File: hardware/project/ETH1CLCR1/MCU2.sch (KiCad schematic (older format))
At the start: 28 parts, among them J1501 Conn_02x05, U1502 24LC08B-E/MS, U501 STM32H743ZI, Y1501 NX3225GD-8MHZ-STD-CRA-3

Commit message: Schematic design
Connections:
- net labels added: SR100CTR, SR10CTR, SR10KCTR, SR1KCTR
- net labels removed: ADC_BUSY, ADC_CLOCK, ADC_CONVST, ADC_MUX_DIN, ADC_MUX_SCLK, ADC_MUX_SDO, ADC_MUX_~SYNC, ADC_RD, ADC_SDI, ADC_SDOA, ADC_~CS, DAC_RSTSEL, DAC_SCLK, DAC_SDIN, DAC_SDO, DAC_~LDAC, DAC_~RESET, DAC_~SYNC, DC_DAC_SCLK, DC_DAC_SDIN, DC_DAC_SDO, DC_DAC_~CLR, DC_DAC_~LDAC, DC_DAC_~SYNC, FOURCE_SELECT, PMU_AC0, PMU_AC1, PMU_AM0, PMU_AM1, PMU_AM2, PMU_CLHDETECT, PMU_CLLDETECT, PMU_CPCK, PMU_CPOH, PMU_CPOL, PMU_CPSEL, PMU_MSEL, PMU_STANDBY, PMU_~CS, PMU_~MOE, PMU_~STB, R_GND, R_GUARD, R_GUARDIN, R_MEASHV, R_MEASIL, R_MEASVL
- wire segments 225 -> 229
- no-connect marks 53 -> 49
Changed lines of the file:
@@
 $Descr A3 16535 11693
 encoding utf-8
-Sheet 6 12
+Sheet 12 13
 Title ""
 Date ""
@@
 Wire Wire Line
 	2900 6300 2850 6300
-Text HLabel 2850 2000 0    50   Output ~ 0
-DC_DAC_~CLR
-Text HLabel 2850 2100 0    50   Output ~ 0
-DC_DAC_~LDAC
-Text HLabel 2850 2400 0    50   Input ~ 0
-DC_DAC_SDO
-Text HLabel 2850 2200 0    50   Output ~ 0
-DC_DAC_~SYNC
-Text HLabel 2850 2300 0    50   Output ~ 0
-DC_DAC_SCLK
-Text HLabel 2850 2500 0    50   Output ~ 0
-DC_DAC_SDIN
 Wire Wire Line
 	2850 2300 2900 2300
@@
 Wire Wire Line
 	2850 2100 2900 2100
-Text HLabel 2850 3900 0    50   Input ~ 0
-ADC_SDOA
-Text HLabel 2850 5400 0    50   Output ~ 0
-ADC_RD
-Text HLabel 2850 4000 0    50   Output ~ 0
-ADC_SDI
-Text HLabel 2850 5500 0    50   Input ~ 0
-ADC_BUSY
-Text HLabel 2850 3800 0    50   Output ~ 0
-ADC_CLOCK
 Wire Wire Line
 	2850 3800 2900 3800
@@
 Text Label 15700 8400 2    50   ~ 0
 MCU_NRST
-Text HLabel 14350 7900 2    50   Output ~ 0
-ADC_MUX_DIN
-Text HLabel 14350 7600 2    50   Output ~ 0
-ADC_MUX_~SYNC
-Text HLabel 14350 7400 2    50   Output ~ 0
-ADC_MUX_SCLK
-Text HLabel 14350 7800 2    50   Input ~ 0
-ADC_MUX_SDO
 Wire Wire Line
 	14350 7600 14300 7600
@@
 Wire Wire Line
 	14300 3700 14350 3700
-Text HLabel 2850 6200 0    50   Output ~ 0
-DAC_SDIN
-Text HLabel 2850 6000 0    50   Output ~ 0
-DAC_SCLK
-Text HLabel 2850 4800 0    50   Output ~ 0
-DAC_~SYNC
 Wire Wire Line
 	1500 1400 2900 1400
-Text HLabel 14350 3800 2    50   Output ~ 0
-PMU_STANDBY
-Text HLabel 14350 3900 2    50   Output ~ 0
-PMU_~STB
-Text HLabel 14350 4000 2    50   Output ~ 0
-PMU_CPCK
-Text HLabel 14350 4100 2    50   Output ~ 0
-PMU_~MOE
-Text HLabel 14350 4200 2    50   Output ~ 0
-PMU_~CS
-Text HLabel 14350 4300 2    50   Output ~ 0
-PMU_AM0
-Text HLabel 14350 4400 2    50   Output ~ 0
-PMU_AM1
-Text HLabel 14350 4500 2    50   Output ~ 0
-PMU_AM2
-Text HLabel 14350 5400 2    50   Output ~ 0
-PMU_CPSEL
-Text HLabel 14350 5500 2    50   Output ~ 0
-PMU_MSEL
-Text HLabel 14350 5600 2    50   Output ~ 0
-PMU_AC0
-Text HLabel 14350 5700 2    50   Output ~ 0
-PMU_AC1
-Text HLabel 14350 5800 2    50   Input ~ 0
-PMU_CPOH
-Text HLabel 14350 5900 2    50   Input ~ 0
-PMU_CPOL
-Text HLabel 14350 6000 2    50   Input ~ 0
-PMU_CLHDETECT
-Text HLabel 14350 6100 2    50   Input ~ 0
-PMU_CLLDETECT
-Text HLabel 14350 1900 2    50   Output ~ 0
-R_MEASIL
-Text HLabel 14350 2000 2    50   Output ~ 0
-R_MEASVL
-Text HLabel 14350 2100 2    50   Output ~ 0
-R_GUARD
-Text HLabel 14350 1600 2    50   Output ~ 0
-R_MEASHV
-Text HLabel 14350 1700 2    50   Output ~ 0
-R_GUARDIN
-Text HLabel 14350 1800 2    50   Output ~ 0
-R_GND
 Wire Wire Line
 	14350 3800 14300 3800
@@
 NoConn ~ 11200 10450
 NoConn ~ 11200 10550
-Text HLabel 14350 6200 2    50   Output ~ 0
-FOURCE_SELECT
 Wire Wire Line
 	14350 6200 14300 6200
@@
 NoConn ~ 2900 4100
 NoConn ~ 2900 4200
-NoConn ~ 2900 5000
-NoConn ~ 2900 5100
-NoConn ~ 2900 5200
-NoConn ~ 2900 5300
 NoConn ~ 2900 5600
 NoConn ~ 2900 5700
@@
 $EndComp
 NoConn ~ 14300 7300
-Text HLabel 2850 4500 0    50   Output ~ 0
-DAC_~RESET
-Text HLabel 2850 4400 0    50   Output ~ 0
-DAC_~LDAC
 Wire Wire Line
 	2850 3700 2900 3700
-Text HLabel 2850 3700 0    50   Output ~ 0
-ADC_~CS
-Text HLabel 2850 6100 0    50   Input ~ 0
-DAC_SDO
 Wire Wire Line
 	2850 6100 2900 6100
@@
 Wire Wire Line
 	2850 4400 2900 4400
-Text HLabel 2850 4300 0    50   Output ~ 0
-DAC_RSTSEL
 Wire Wire Line
 	2850 4300 2900 4300
@@
 Wire Wire Line
 	2850 8600 2900 8600
-Text HLabel 14350 6400 2    50   Output ~ 0
-ADC_CONVST
 Wire Wire Line
 	14350 6400 14300 6400
 NoConn ~ 14300 6500
+Text HLabel 2850 5100 0    50   Output ~ 0
+SR1KCTR
+Text HLabel 2850 5000 0    50   Output ~ 0
+SR10KCTR
+Text HLabel 2850 5300 0    50   Output ~ 0
+SR10CTR
+Text HLabel 2850 5200 0    50   Output ~ 0
+SR100CTR
+Wire Wire Line
+	2850 5300 2900 5300
+Wire Wire Line
+	2900 5200 2850 5200
+Wire Wire Line
+	2850 5100 2900 5100
+Wire Wire Line
+	2900 5000 2850 5000
 $EndSCHEMATC

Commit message: Schematic design
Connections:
- net labels added: +3.3VP, ADC_BUSY, ADC_CLOCK, ADC_CONVST, ADC_NULL1, ADC_NULL2, ADC_RD, ADC_SDI, ADC_SDOA, ADC_~CS, CXN_RELA, CXN_RELB, CXN_RELC, CXN_RELD, CXN_RELE, CXN_RELF, DAC1_LDAC, DAC1_~ENABLE, DAC2_LDAC, DAC2_~ENABLE, DAC_DIN, DAC_SCLK, DAC_~SYNC, FB_CLK, FB_RDY, FB_SDI, FB_SDO, FB_~CS, FB_~RST, G1A0_CTR, G1A1_CTR, G2A0_CTR, G2A1_CTR, HA3-COMP, PA_50MV, PA_EM, PA_MOS1, PA_MOS2, PA_MOS3, PA_MOS4, PA_MOS5, PA_MOS6, PA_NULL, R100CRT, R100KCRT, R10CRT, R10KCRT, R1KCRT, RELAY_CTR, RR_CLK, RR_RDY, RR_SDI, RR_SDO, RR_~CS, RR_~RST
- wire segments 229 -> 233
- no-connect marks 49 -> 45
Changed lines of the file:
@@
 $Descr A3 16535 11693
 encoding utf-8
-Sheet 12 14
+Sheet 11 16
 Title ""
 Date ""
@@
 Comment4 ""
 $EndDescr
-$Comp
-L ETH1CLCR1:STM32H743ZI U501
-U 1 1 5DD1F48B
-P 8600 5050
-F 0 "U501" H 3150 8950 50  0000 C CNN
-F 1 "STM32H743ZI" H 13850 8950 50  0000 C CNN
-F 2 "ETH1CLCR1:TQFP-144_20x20mm_P0.5mm" H 24500 6550 50  0001 C CNN
-F 3 "" H 24500 6550 50  0001 C CNN
-	1    8600 5050
-	1    0    0    -1
-$EndComp
-$Comp
-L ETH1CLCR1:+3.3VF #PWR0501
-U 1 1 5DD24561
-P 8600 900
-F 0 "#PWR0501" H 8600 750 50  0001 C CNN
-F 1 "+3.3VF" H 8615 1073 50  0000 C CNN
-F 2 "" H 8600 900 50  0001 C CNN
-F 3 "" H 8600 900 50  0001 C CNN
-	1    8600 900
-	1    0    0    -1
-$EndComp
 Wire Wire Line
 	7400 1000 7400 950
@@
 F 3 "" H 10550 10700 50  0001 C CNN
 	1    10550 10700
-	1    0    0    -1
-$EndComp
-$Comp
-L ETH1CLCR1:+3.3VF #PWR0512
-U 1 1 5DD9082D
-P 10550 10150
-F 0 "#PWR0512" H 10550 10000 50  0001 C CNN
-F 1 "+3.3VF" H 10565 10323 50  0000 C CNN
-F 2 "" H 10550 10150 50  0001 C CNN
-F 3 "" H 10550 10150 50  0001 C CNN
-	1    10550 10150
 	1    0    0    -1
 $EndComp
@@
 $EndComp
 $Comp
-L ETH1CLCR1:+3.3VF #PWR0513
-U 1 1 5E23D8BE
-P 8500 10200
-F 0 "#PWR0513" H 8500 10050 50  0001 C CNN
-F 1 "+3.3VF" H 8515 10373 50  0000 C CNN
-F 2 "" H 8500 10200 50  0001 C CNN
-F 3 "" H 8500 10200 50  0001 C CNN
-	1    8500 10200
-	1    0    0    -1
-$EndComp
-$Comp
-L ETH1CLCR1:+3.3VF #PWR0511
-U 1 1 5E23DAAC
-P 9800 9950
-F 0 "#PWR0511" H 9800 9800 50  0001 C CNN
-F 1 "+3.3VF" H 9815 10123 50  0000 C CNN
-F 2 "" H 9800 9950 50  0001 C CNN
-F 3 "" H 9800 9950 50  0001 C CNN
-	1    9800 9950
-	1    0    0    -1
-$EndComp
-$Comp
 L Device:C C?
 U 1 1 5E25BB78
@@
 Wire Wire Line
 	3400 10450 3650 10450
-$Comp
-L ETH1CLCR1:+3.3VF #PWR0515
-U 1 1 5DFCC179
-P 3400 10400
-F 0 "#PWR0515" H 3400 10250 50  0001 C CNN
-F 1 "+3.3VF" H 3415 10573 50  0000 C CNN
-F 2 "" H 3400 10400 50  0001 C CNN
-F 3 "" H 3400 10400 50  0001 C CNN
-	1    3400 10400
-	1    0    0    -1
-$EndComp
 $Comp
 L ETH1CLCR1:DGNDF #PWR0520
@@
 Wire Wire Line
 	14350 7800 14300 7800
-$Comp
-L ETH1CLCR1:+3.3VF #PWR0503
-U 1 1 5E8AA48C
-P 15200 8050
-F 0 "#PWR0503" H 15200 7900 50  0001 C CNN
-F 1 "+3.3VF" H 15215 8223 50  0000 C CNN
-F 2 "" H 15200 8050 50  0001 C CNN
-F 3 "" H 15200 8050 50  0001 C CNN
-	1    15200 8050
-	1    0    0    -1
-$EndComp
 Wire Wire Line
 	14350 7900 14300 7900
@@
 Wire Wire Line
 	15200 8400 14300 8400
-NoConn ~ 2900 1600
-NoConn ~ 2900 1700
-NoConn ~ 2900 1800
-NoConn ~ 2900 1900
 NoConn ~ 2900 2600
 NoConn ~ 2900 2700
@@
 MCU_VDDA
 $Comp
-L ETH1CLCR1:+3.3VF #PWR0514
-U 1 1 5E2EEABF
-P 6600 10350
-F 0 "#PWR0514" H 6600 10200 50  0001 C CNN
-F 1 "+3.3VF" H 6615 10523 50  0000 C CNN
-F 2 "" H 6600 10350 50  0001 C CNN
-F 3 "" H 6600 10350 50  0001 C CNN
-	1    6600 10350
-	1    0    0    -1
-$EndComp
-$Comp
 L ETH1CLCR1:DGNDF #PWR0517
 U 1 1 5E2F2EC2
@@
 Wire Wire Line
 	2900 5000 2850 5000
+$Comp
+L power:+3.3VP #PWR01203
+U 1 1 5E6F8C8C
+P 8600 900
+F 0 "#PWR01203" H 8750 850 50  0001 C CNN
+F 1 "+3.3VP" H 8620 1043 50  0000 C CNN
+F 2 "" H 8600 900 50  0001 C CNN
+F 3 "" H 8600 900 50  0001 C CNN
+	1    8600 900
+	1    0    0    -1
+$EndComp
+$Comp
+L power:+3.3VP #PWR01216
+U 1 1 5E6F95E8
+P 15200 8050
+F 0 "#PWR01216" H 15350 8000 50  0001 C CNN
+F 1 "+3.3VP" H 15220 8193 50  0000 C CNN
+F 2 "" H 15200 8050 50  0001 C CNN
+F 3 "" H 15200 8050 50  0001 C CNN
+	1    15200 8050
+	1    0    0    -1
+$EndComp
+$Comp
+L power:+3.3VP #PWR01201
+U 1 1 5E70083D
+P 6600 10350
+F 0 "#PWR01201" H 6750 10300 50  0001 C CNN
+F 1 "+3.3VP" H 6620 10493 50  0000 C CNN
+F 2 "" H 6600 10350 50  0001 C CNN
+F 3 "" H 6600 10350 50  0001 C CNN
+	1    6600 10350
+	1    0    0    -1
+$EndComp
+$Comp
+L power:+3.3VP #PWR01202
+U 1 1 5E703151
+P 8500 10200
+F 0 "#PWR01202" H 8650 10150 50  0001 C CNN
+F 1 "+3.3VP" H 8520 10343 50  0000 C CNN
+F 2 "" H 8500 10200 50  0001 C CNN
+F 3 "" H 8500 10200 50  0001 C CNN
+	1    8500 10200
+	1    0    0    -1
+$EndComp
+$Comp
+L power:+3.3VP #PWR01205
+U 1 1 5E703CD5
+P 9800 9950
+F 0 "#PWR01205" H 9950 9900 50  0001 C CNN
+F 1 "+3.3VP" H 9820 10093 50  0000 C CNN
+F 2 "" H 9800 9950 50  0001 C CNN
+F 3 "" H 9800 9950 50  0001 C CNN
+	1    9800 9950
+	1    0    0    -1
+$EndComp
+$Comp
+L power:+3.3VP #PWR01215
+U 1 1 5E705830
+P 10550 10150
+F 0 "#PWR01215" H 10700 10100 50  0001 C CNN
+F 1 "+3.3VP" H 10570 10293 50  0000 C CNN
+F 2 "" H 10550 10150 50  0001 C CNN
+F 3 "" H 10550 10150 50  0001 C CNN
+	1    10550 10150
+	1    0    0    -1
+$EndComp
+$Comp
+L ETH1CLCR1:STM32H743ZI U501
+U 1 1 5DD1F48B
+P 8600 5050
+F 0 "U501" H 3150 8950 50  0000 C CNN
+F 1 "STM32H743ZI" H 13850 8950 50  0000 C CNN
+F 2 "ETH1CLCR1:TQFP-144_20x20mm_P0.5mm" H 24500 6550 50  0001 C CNN
+F 3 "" H 24500 6550 50  0001 C CNN
+	1    8600 5050
+	1    0    0    -1
+$EndComp
+Wire Wire Line
+	2900 1900 2850 1900
+Wire Wire Line
+	2850 1800 2900 1800
+Wire Wire Line
+	2900 1700 2850 1700
+Wire Wire Line
+	2850 1600 2900 1600
+Text HLabel 2850 1600 0    50   Output ~ 0
+CXN_RELA
+Text HLabel 2850 1700 0    50   Output ~ 0
+CXN_RELB
+Text HLabel 2850 1800 0    50   Output ~ 0
+CXN_RELC
+Text HLabel 2850 1900 0    50   Output ~ 0
+CXN_RELD
+Text HLabel 2850 2000 0    50   Output ~ 0
+CXN_RELE
+Text HLabel 2850 2100 0    50   Output ~ 0
+CXN_RELF
+Text HLabel 1050 3450 0    50   Output ~ 0
+R100CRT
+Text HLabel 1050 3350 0    50   Output ~ 0
+R10CRT
+Text HLabel 1050 3550 0    50   Output ~ 0
+R1KCRT
+Text HLabel 1050 3650 0    50   Output ~ 0
+R10KCRT
+Text HLabel 1050 3750 0    50   Output ~ 0
+R100KCRT
+Text HLabel 1050 3850 0    50   Output ~ 0
+RELAY_CTR
+Text HLabel 1050 3950 0    50   Output ~ 0
+HA3-COMP
+Text HLabel 1050 4250 0    50   Output ~ 0
+PA_NULL
+Text HLabel 1050 4350 0    50   Output ~ 0
+PA_EM
+Text HLabel 1050 4450 0    50   Output ~ 0
+PA_50MV
+Text HLabel 1050 4550 0    50   Output ~ 0
+PA_MOS1
+Text HLabel 1050 4650 0    50   Output ~ 0
+PA_MOS2
+Text HLabel 1050 4750 0    50   Output ~ 0
+PA_MOS3
+Text HLabel 1050 4850 0    50   Output ~ 0
+PA_MOS4
+Text HLabel 1050 4950 0    50   Output ~ 0
+PA_MOS5
+Text HLabel 1050 5050 0    50   Output ~ 0
+PA_MOS6
+Text HLabel 1050 5250 0    50   Output ~ 0
+DAC_~SYNC
+Text HLabel 1050 5350 0    50   Output ~ 0
+DAC_SCLK
+Text HLabel 1050 5450 0    50   Output ~ 0
+DAC_DIN
+Text HLabel 1050 5550 0    50   Output ~ 0
+DAC1_~ENABLE
+Text HLabel 1050 5650 0    50   Output ~ 0
+DAC1_LDAC
+Text HLabel 1050 5750 0    50   Output ~ 0
+DAC2_~ENABLE
+Text HLabel 1050 5850 0    50   Output ~ 0
+DAC2_LDAC
+Text HLabel 1050 6050 0    50   Output ~ 0
+G1A1_CTR
+Text HLabel 1050 6150 0    50   Output ~ 0
+G1A0_CTR
+Text HLabel 1050 6250 0    50   Output ~ 0
+G2A1_CTR
+Text HLabel 1050 6350 0    50   Output ~ 0
+G2A0_CTR
+Text HLabel 1050 6600 0    50   Output ~ 0
+ADC_NULL2
+Text HLabel 1050 6700 0    50   Output ~ 0
+ADC_NULL1
+Text HLabel 1050 7500 0    50   Output ~ 0
+ADC_CONVST
+Text HLabel 1050 6900 0    50   Output ~ 0
+ADC_~CS
+Text HLabel 1050 7000 0    50   Output ~ 0
+ADC_CLOCK
+Text HLabel 1050 7100 0    50   Input ~ 0
+ADC_BUSY
+Text HLabel 1050 7200 0    50   Output ~ 0
+ADC_SDI
+Text HLabel 1050 7300 0    50   Output ~ 0
+ADC_RD
+Text HLabel 1050 7400 0    50   Input ~ 0
+ADC_SDOA
+Text HLabel 1050 7700 0    50   Output ~ 0
+RR_SDI
+Text HLabel 1050 7800 0    50   Input ~ 0
+RR_SDO
+Text HLabel 1050 7900 0    50   Output ~ 0
+RR_CLK
+Text HLabel 1050 8000 0    50   Output ~ 0
+RR_~CS
+Text HLabel 1050 8100 0    50   Input ~ 0
+RR_RDY
+Text HLabel 1050 8200 0    50   Output ~ 0
+RR_~RST
+Text HLabel 1050 8400 0    50   Output ~ 0
+FB_SDI
+Text HLabel 1050 8500 0    50   Input ~ 0
+FB_SDO
+Text HLabel 1050 8600 0    50   Output ~ 0
+FB_CLK
+Text HLabel 1050 8700 0    50   Output ~ 0
+FB_~CS
+Text HLabel 1050 8800 0    50   Input ~ 0
+FB_RDY
+Text HLabel 1050 8900 0    50   Output ~ 0
+FB_~RST
 $EndSCHEMATC

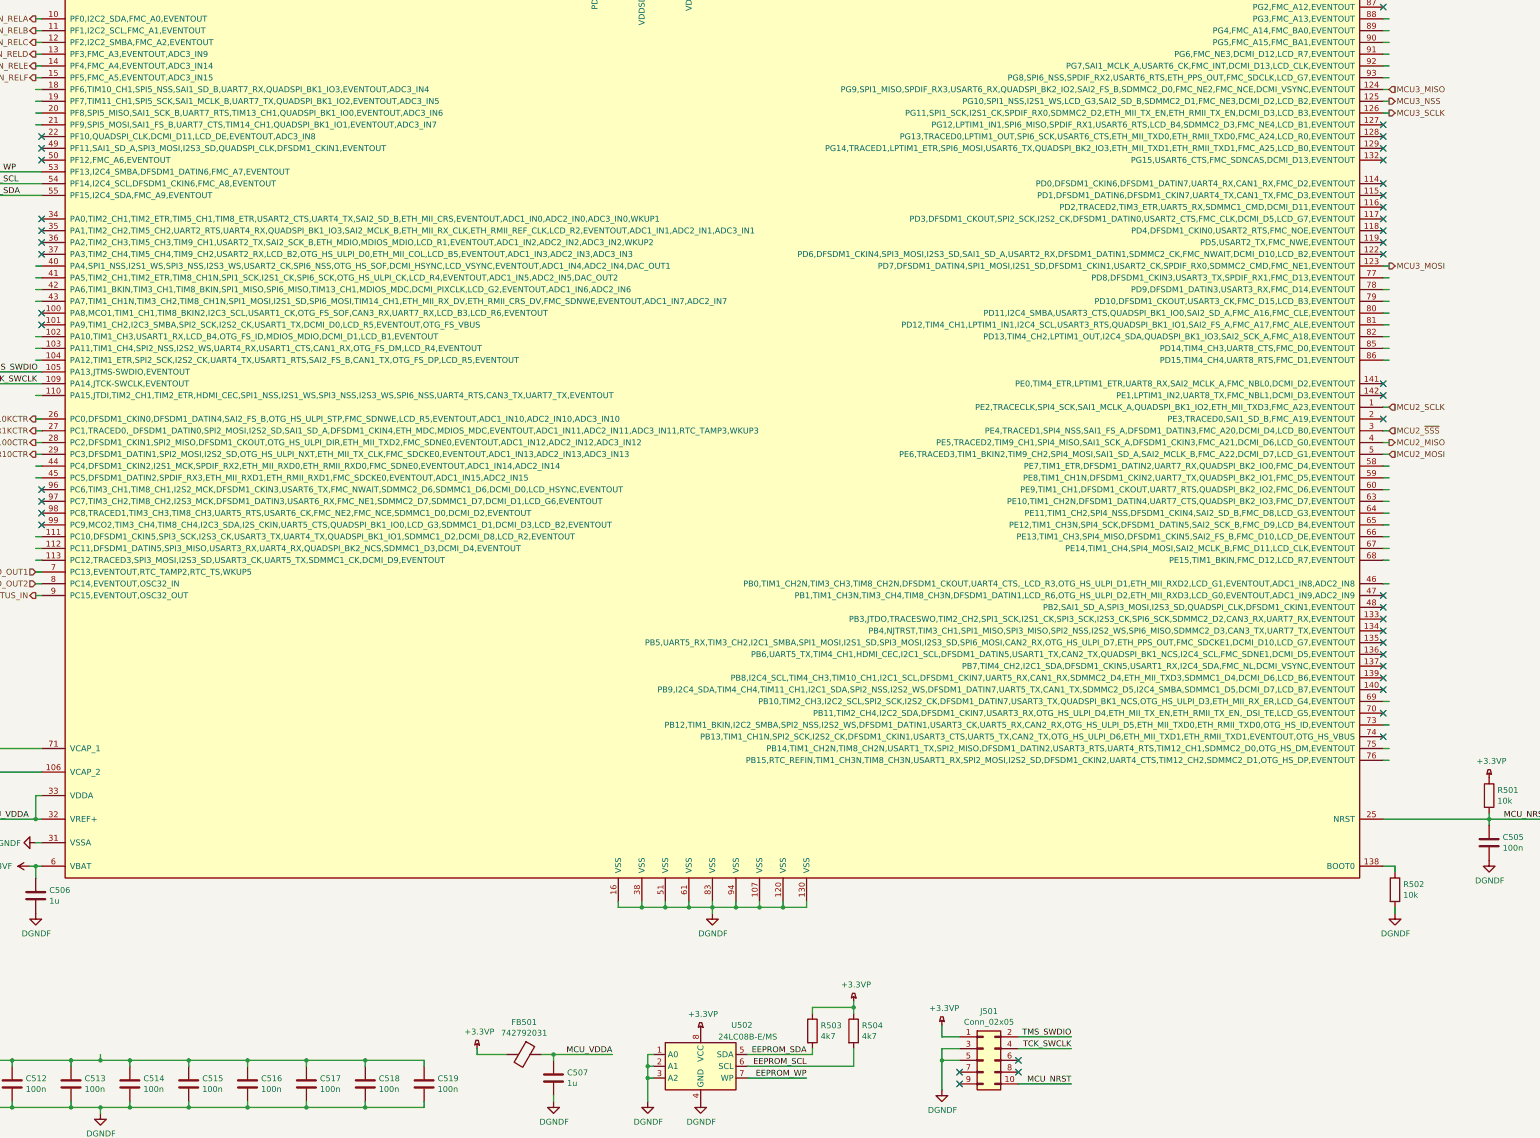
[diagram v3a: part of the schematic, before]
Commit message: Need to redesign the AC source, the LT1468 is too slow.
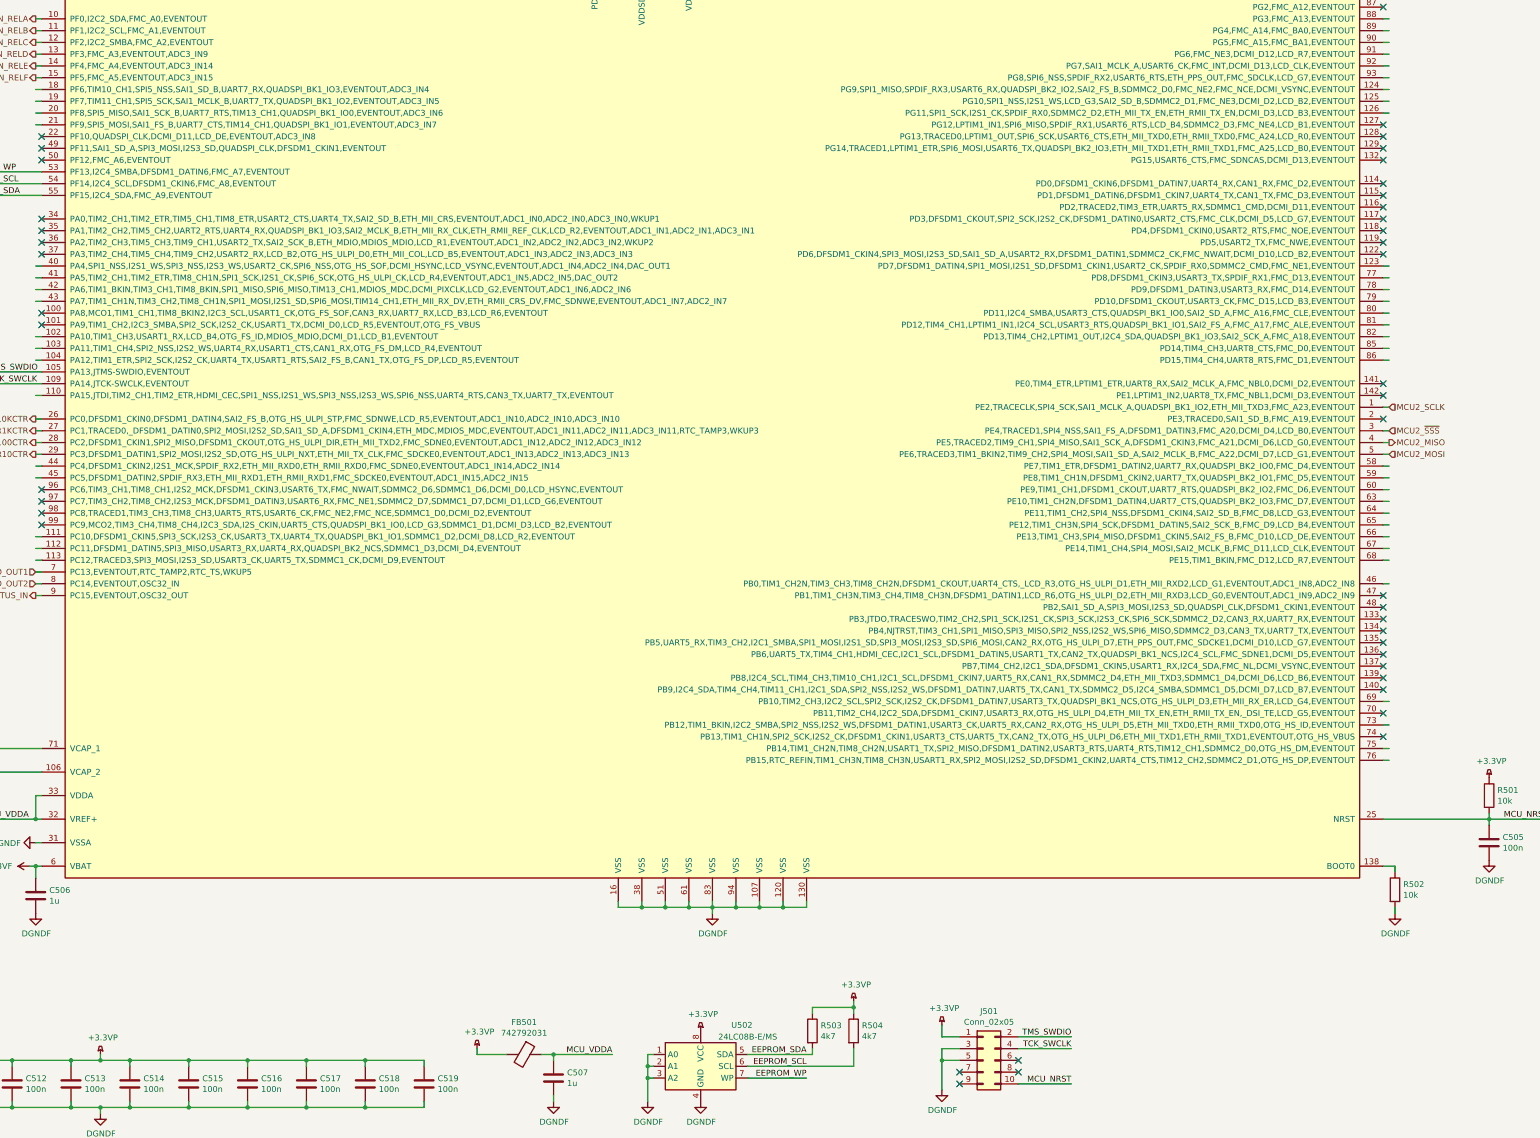
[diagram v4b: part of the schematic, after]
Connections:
- net labels removed: MCU3_MISO, MCU3_MOSI, MCU3_NSS, MCU3_SCLK
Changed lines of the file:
@@
 Wire Wire Line
 	2850 4300 2900 4300
-Text HLabel 14350 2300 2    50   Output ~ 0
-MCU3_NSS
-Text HLabel 14350 2400 2    50   Output ~ 0
-MCU3_SCLK
-Text HLabel 14350 2200 2    50   Input ~ 0
-MCU3_MISO
-Text HLabel 14350 3700 2    50   Output ~ 0
-MCU3_MOSI
 NoConn ~ 14300 3000
 NoConn ~ 14300 3100
@@
 Text HLabel 1050 8900 0    50   Output ~ 0
 FB_~RST
+$Comp
+L power:+3.3VP #PWR0130
+U 1 1 5E157C4F
+P 3400 10400
+F 0 "#PWR0130" H 3550 10350 50  0001 C CNN
+F 1 "+3.3VP" H 3420 10543 50  0000 C CNN
+F 2 "" H 3400 10400 50  0001 C CNN
+F 3 "" H 3400 10400 50  0001 C CNN
+	1    3400 10400
+	1    0    0    -1
+$EndComp
 $EndSCHEMATC

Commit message: Footprint asigment (not finished).
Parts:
- C1106: renamed from C1506; footprint Capacitor_SMD:C_0603_1608Metric_Pad1.05x0.95mm_HandSolder -> Capacitor_SMD:C_0805_2012Metric_Pad1.15x1.40mm_HandSolder
- C1107: renamed from C1507; footprint Capacitor_SMD:C_0603_1608Metric_Pad1.05x0.95mm_HandSolder -> Capacitor_SMD:C_0805_2012Metric_Pad1.15x1.40mm_HandSolder
- renumbered C1501 to C1101, C1502 to C1102, C1503 to C1103, C1504 to C1104, C1505 to C1105, C508 to C1108, C509 to C1109, C510 to C1110, C511 to C1111, C512 to C1112, C513 to C1113, C514 to C1114, C515 to C1115, C516 to C1116, C517 to C1117, C518 to C1118, C519 to C1119, FB1501 to FB1101, J1501 to J1101, R1501 to R1101, R502 to R1102, R1503 to R1103, R1504 to R1104, U501 to U1101, U1502 to U1102, Y1501 to Y1101
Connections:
- net labels added: DAC_~CLR, DAC_~LDAC, FB_CAP
- net labels removed: DAC1_LDAC, DAC1_~ENABLE, DAC2_LDAC, DAC2_~ENABLE

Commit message: Modification in schematic and PCB layout.
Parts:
- C1106, C1107: footprint Capacitor_SMD:C_0805_2012Metric_Pad1.15x1.40mm_HandSolder -> Capacitor_SMD:C_0603_1608Metric_Pad1.05x0.95mm_HandSolder
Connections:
- net labels added: CXN_REL1, CXN_REL2, CXN_REL3, CXN_REL4, CXN_REL5, CXN_REL6, MCU3_MISO, MCU3_MOSI, MCU3_NSS, MCU3_SCLK
- net labels removed: +3.3VF, CXN_RELA, CXN_RELB, CXN_RELC, CXN_RELD, CXN_RELE, CXN_RELF
- wire segments 233 -> 235
- no-connect marks 45 -> 43

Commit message: Redesinged ADC schematic.
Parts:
- renumbered C1108 to C1101, C1101 to C1102, C1109 to C1103, C1102 to C1104, C1110 to C1105, C1103 to C1106, C1104 to C1107, C1111 to C1108, C1112 to C1109, C1106 to C1110, C1113 to C1111, C1114 to C1112, C1115 to C1113, C1116 to C1114, C1117 to C1115, C1118 to C1116, C1119 to C1117, C1107 to C1118, C1105 to C1119, R1103 to R1101, R1104 to R1102, R1102 to R1103, R1101 to R1104, U1102 to U1101, U1101 to U1102

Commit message: Redesigned the power supply, added humidy+temp. sensor.
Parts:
- renumbered C1101 to C1301, C1102 to C1302, C1103 to C1303, C1104 to C1304, C1105 to C1305, C1106 to C1306, C1107 to C1307, C1108 to C1308, C1109 to C1309, C1110 to C1310, C1111 to C1311, C1112 to C1312, C1113 to C1313, C1114 to C1314, C1115 to C1315, C1116 to C1316, C1117 to C1317, C1118 to C1318, C1119 to C1319, FB1101 to FB1301, J1101 to J1301, R1101 to R1301, R1102 to R1302, R1103 to R1303, R1104 to R1304, U1101 to U1301, U1102 to U1302, Y1101 to Y1301
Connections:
- net ADC_BUSY renamed ADC_~ALARM
- net ADC_CLOCK renamed ADC_SCLK
- net ADC_CONVST: no longer names the net of U1302.35 (PA1,TIM2_CH2,TIM5_CH2,UART2_RTS,UART4_RX,QUADSPI_BK1_IO3,SAI2_MCLK_B,ETH_MII_RX_CLK,ETH_RMII_REF_CLK,LCD_R2,EVENTOUT,ADC1_IN1,ADC2_IN1,ADC3_IN1)
- net ADC_RD: no longer names the net of U1302.36 (PA2,TIM2_CH3,TIM5_CH3,TIM9_CH1,USART2_TX,SAI2_SCK_B,ETH_MDIO,MDIOS_MDIO,LCD_R1,EVENTOUT,ADC1_IN2,ADC2_IN2,ADC3_IN2,WKUP2)
- net MCU2_GPIO_OUT1 renamed MCU1_GPIO_OUT1
- net MCU2_GPIO_OUT2 renamed MCU1_GPIO_OUT2
- net MCU2_MISO renamed MCU1_MISO
- net MCU2_MOSI renamed MCU1_MOSI
- net MCU2_SCLK renamed MCU1_SCLK
- net MCU2_STATUS_IN renamed MCU1_STATUS_IN
- net MCU2_~SSS renamed MCU1_~SS
- no-connect marks 43 -> 45
